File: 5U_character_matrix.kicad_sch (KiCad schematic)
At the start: 14 parts, among them U1 SN74LVC244A, U2 SM411006N/15, U3 SM411006N/15, U4 SN74LVC244A, U5 SM411006N/15, U6 SM411006N/15, U7 SM411006N/15

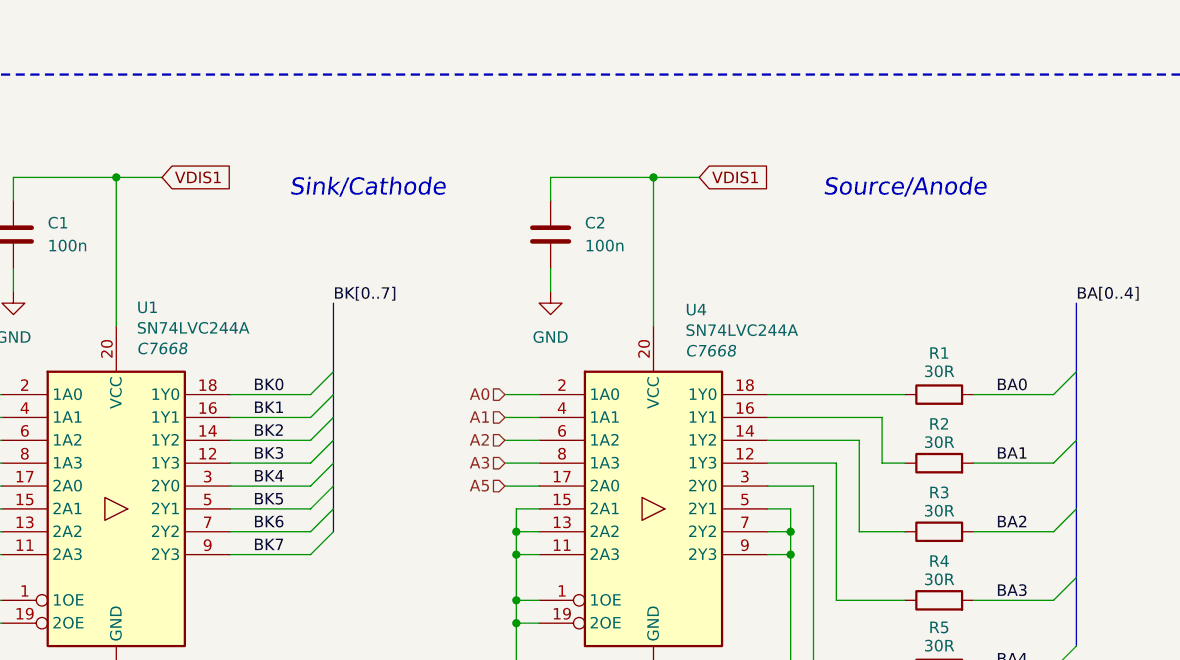
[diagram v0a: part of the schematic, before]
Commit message: power circuit added
- addition of power circuit
- added bypassing circuit
- new formatting of the schematic
- root schematic updated
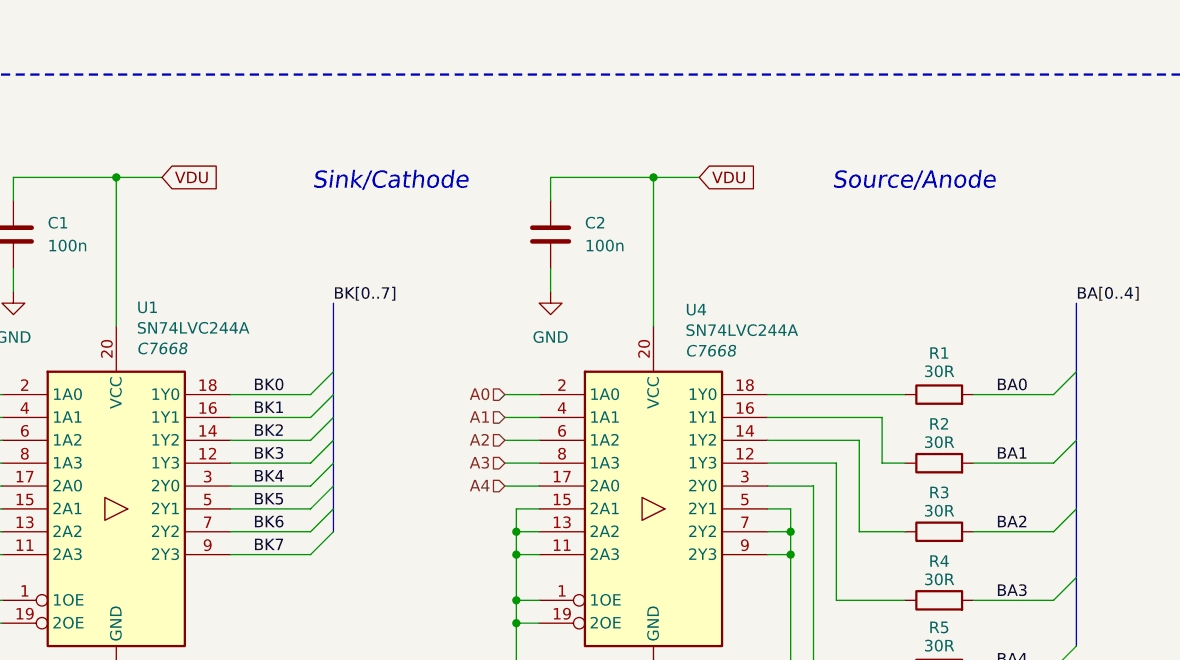
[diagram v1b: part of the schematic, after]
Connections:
- net A5 renamed A4
- net VDIS1 renamed VDU
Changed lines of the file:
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@@
 	(text "Sink/Cathode "
 		(exclude_from_sim no)
-		(at 76.2 114.3 0)
+		(at 78.74 113.538 0)
 		(effects
 			(font
@@
 				(thickness 0.2381)
 				(italic yes)
-				(color 194 0 0 1)
+				(color 132 0 0 1)
 			)
 		)
@@
 	(text "Source/Anode"
 		(exclude_from_sim no)
-		(at 135.89 114.3 0)
+		(at 136.906 113.538 0)
 		(effects
 			(font
@@
 				(thickness 0.2381)
 				(italic yes)
-				(color 194 0 0 1)
+				(color 132 0 0 1)
 			)
 		)
@@
 		)
 	)
-	(global_label "VDIS1"
+	(global_label "VDU"
 		(shape input)
 		(at 113.03 113.03 0)
@@
 		)
 		(property "Intersheetrefs" "${INTERSHEET_REFS}"
-			(at 121.3976 113.03 0)
+			(at 119.7043 113.03 0)
 			(effects
 				(font
@@
 		)
 	)
-	(global_label "VDIS1"
+	(global_label "VDU"
 		(shape input)
 		(at 53.34 113.03 0)
@@
 		)
 		(property "Intersheetrefs" "${INTERSHEET_REFS}"
-			(at 61.7076 113.03 0)
+			(at 60.0143 113.03 0)
 			(effects
 				(font
@@
 		)
 	)
-	(hierarchical_label "A5"
+	(hierarchical_label "A4"
 		(shape input)
 		(at 91.44 147.32 180)
@@
 		(instances
 			(project "Precision Clock"
-				(path "/c9a8ff63-a0d1-4125-9dd1-40fb53daf536/61b252ee-6ab4-4417-a4ad-7fc052d7ca20"
-					(reference "R14")
-					(unit 1)
-				)
 				(path "/c9a8ff63-a0d1-4125-9dd1-40fb53daf536/95a63663-b2f9-448f-a4dd-b71321e8f379"
 					(reference "R4")
@@
 		(instances
 			(project "Precision Clock"
-				(path "/c9a8ff63-a0d1-4125-9dd1-40fb53daf536/61b252ee-6ab4-4417-a4ad-7fc052d7ca20"
-					(reference "U17")
-					(unit 1)
-				)
 				(path "/c9a8ff63-a0d1-4125-9dd1-40fb53daf536/95a63663-b2f9-448f-a4dd-b71321e8f379"
 					(reference "U3")
@@
 		(instances
 			(project "Precision Clock"
-				(path "/c9a8ff63-a0d1-4125-9dd1-40fb53daf536/61b252ee-6ab4-4417-a4ad-7fc052d7ca20"
-					(reference "C5")
-					(unit 1)
-				)
 				(path "/c9a8ff63-a0d1-4125-9dd1-40fb53daf536/95a63663-b2f9-448f-a4dd-b71321e8f379"
 					(reference "C1")
@@
 		(instances
 			(project "Precision Clock"
-				(path "/c9a8ff63-a0d1-4125-9dd1-40fb53daf536/61b252ee-6ab4-4417-a4ad-7fc052d7ca20"
-					(reference "C6")
-					(unit 1)
-				)
 				(path "/c9a8ff63-a0d1-4125-9dd1-40fb53daf536/95a63663-b2f9-448f-a4dd-b71321e8f379"
 					(reference "C2")
@@
 		(instances
 			(project "Precision Clock"
-				(path "/c9a8ff63-a0d1-4125-9dd1-40fb53daf536/61b252ee-6ab4-4417-a4ad-7fc052d7ca20"
-					(reference "U20")
-					(unit 1)
-				)
 				(path "/c9a8ff63-a0d1-4125-9dd1-40fb53daf536/95a63663-b2f9-448f-a4dd-b71321e8f379"
 					(reference "U6")
@@
 		(instances
 			(project "Precision Clock"
-				(path "/c9a8ff63-a0d1-4125-9dd1-40fb53daf536/61b252ee-6ab4-4417-a4ad-7fc052d7ca20"
-					(reference "#PWR09")
-					(unit 1)
-				)
 				(path "/c9a8ff63-a0d1-4125-9dd1-40fb53daf536/95a63663-b2f9-448f-a4dd-b71321e8f379"
 					(reference "#PWR01")
@@
 		(instances
 			(project "Precision Clock"
-				(path "/c9a8ff63-a0d1-4125-9dd1-40fb53daf536/61b252ee-6ab4-4417-a4ad-7fc052d7ca20"
-					(reference "R12")
-					(unit 1)
-				)
 				(path "/c9a8ff63-a0d1-4125-9dd1-40fb53daf536/95a63663-b2f9-448f-a4dd-b71321e8f379"
 					(reference "R2")
@@
 		(instances
 			(project "Precision Clock"
-				(path "/c9a8ff63-a0d1-4125-9dd1-40fb53daf536/61b252ee-6ab4-4417-a4ad-7fc052d7ca20"
-					(reference "U19")
-					(unit 1)
-				)
 				(path "/c9a8ff63-a0d1-4125-9dd1-40fb53daf536/95a63663-b2f9-448f-a4dd-b71321e8f379"
 					(reference "U5")
@@
 		(instances
 			(project "Precision Clock"
-				(path "/c9a8ff63-a0d1-4125-9dd1-40fb53daf536/61b252ee-6ab4-4417-a4ad-7fc052d7ca20"
-					(reference "U15")
-					(unit 1)
-				)
 				(path "/c9a8ff63-a0d1-4125-9dd1-40fb53daf536/95a63663-b2f9-448f-a4dd-b71321e8f379"
 					(reference "U1")
@@
 		(instances
 			(project "Precision Clock"
-				(path "/c9a8ff63-a0d1-4125-9dd1-40fb53daf536/61b252ee-6ab4-4417-a4ad-7fc052d7ca20"
-					(reference "#PWR011")
-					(unit 1)
-				)
 				(path "/c9a8ff63-a0d1-4125-9dd1-40fb53daf536/95a63663-b2f9-448f-a4dd-b71321e8f379"
 					(reference "#PWR03")
@@
 		(instances
 			(project "Precision Clock"
-				(path "/c9a8ff63-a0d1-4125-9dd1-40fb53daf536/61b252ee-6ab4-4417-a4ad-7fc052d7ca20"
-					(reference "U18")
-					(unit 1)
-				)
 				(path "/c9a8ff63-a0d1-4125-9dd1-40fb53daf536/95a63663-b2f9-448f-a4dd-b71321e8f379"
 					(reference "U4")
@@
 		(instances
 			(project "Precision Clock"
-				(path "/c9a8ff63-a0d1-4125-9dd1-40fb53daf536/61b252ee-6ab4-4417-a4ad-7fc052d7ca20"
-					(reference "#PWR010")
-					(unit 1)
-				)
 				(path "/c9a8ff63-a0d1-4125-9dd1-40fb53daf536/95a63663-b2f9-448f-a4dd-b71321e8f379"
 					(reference "#PWR02")
@@
 		(instances
 			(project "Precision Clock"
-				(path "/c9a8ff63-a0d1-4125-9dd1-40fb53daf536/61b252ee-6ab4-4417-a4ad-7fc052d7ca20"
-					(reference "R15")
-					(unit 1)
-				)
 				(path "/c9a8ff63-a0d1-4125-9dd1-40fb53daf536/95a63663-b2f9-448f-a4dd-b71321e8f379"
 					(reference "R5")
@@
 		(instances
 			(project "Precision Clock"
-				(path "/c9a8ff63-a0d1-4125-9dd1-40fb53daf536/61b252ee-6ab4-4417-a4ad-7fc052d7ca20"
-					(reference "#PWR012")
-					(unit 1)
-				)
 				(path "/c9a8ff63-a0d1-4125-9dd1-40fb53daf536/95a63663-b2f9-448f-a4dd-b71321e8f379"
 					(reference "#PWR04")
@@
 		(instances
 			(project "Precision Clock"
-				(path "/c9a8ff63-a0d1-4125-9dd1-40fb53daf536/61b252ee-6ab4-4417-a4ad-7fc052d7ca20"
-					(reference "U21")
-					(unit 1)
-				)
 				(path "/c9a8ff63-a0d1-4125-9dd1-40fb53daf536/95a63663-b2f9-448f-a4dd-b71321e8f379"
 					(reference "U7")
@@
 		(instances
 			(project "Precision Clock"
-				(path "/c9a8ff63-a0d1-4125-9dd1-40fb53daf536/61b252ee-6ab4-4417-a4ad-7fc052d7ca20"
-					(reference "R11")
-					(unit 1)
-				)
 				(path "/c9a8ff63-a0d1-4125-9dd1-40fb53daf536/95a63663-b2f9-448f-a4dd-b71321e8f379"
 					(reference "R1")
@@
 		(instances
 			(project "Precision Clock"
-				(path "/c9a8ff63-a0d1-4125-9dd1-40fb53daf536/61b252ee-6ab4-4417-a4ad-7fc052d7ca20"
-					(reference "R13")
-					(unit 1)
-				)
 				(path "/c9a8ff63-a0d1-4125-9dd1-40fb53daf536/95a63663-b2f9-448f-a4dd-b71321e8f379"
 					(reference "R3")

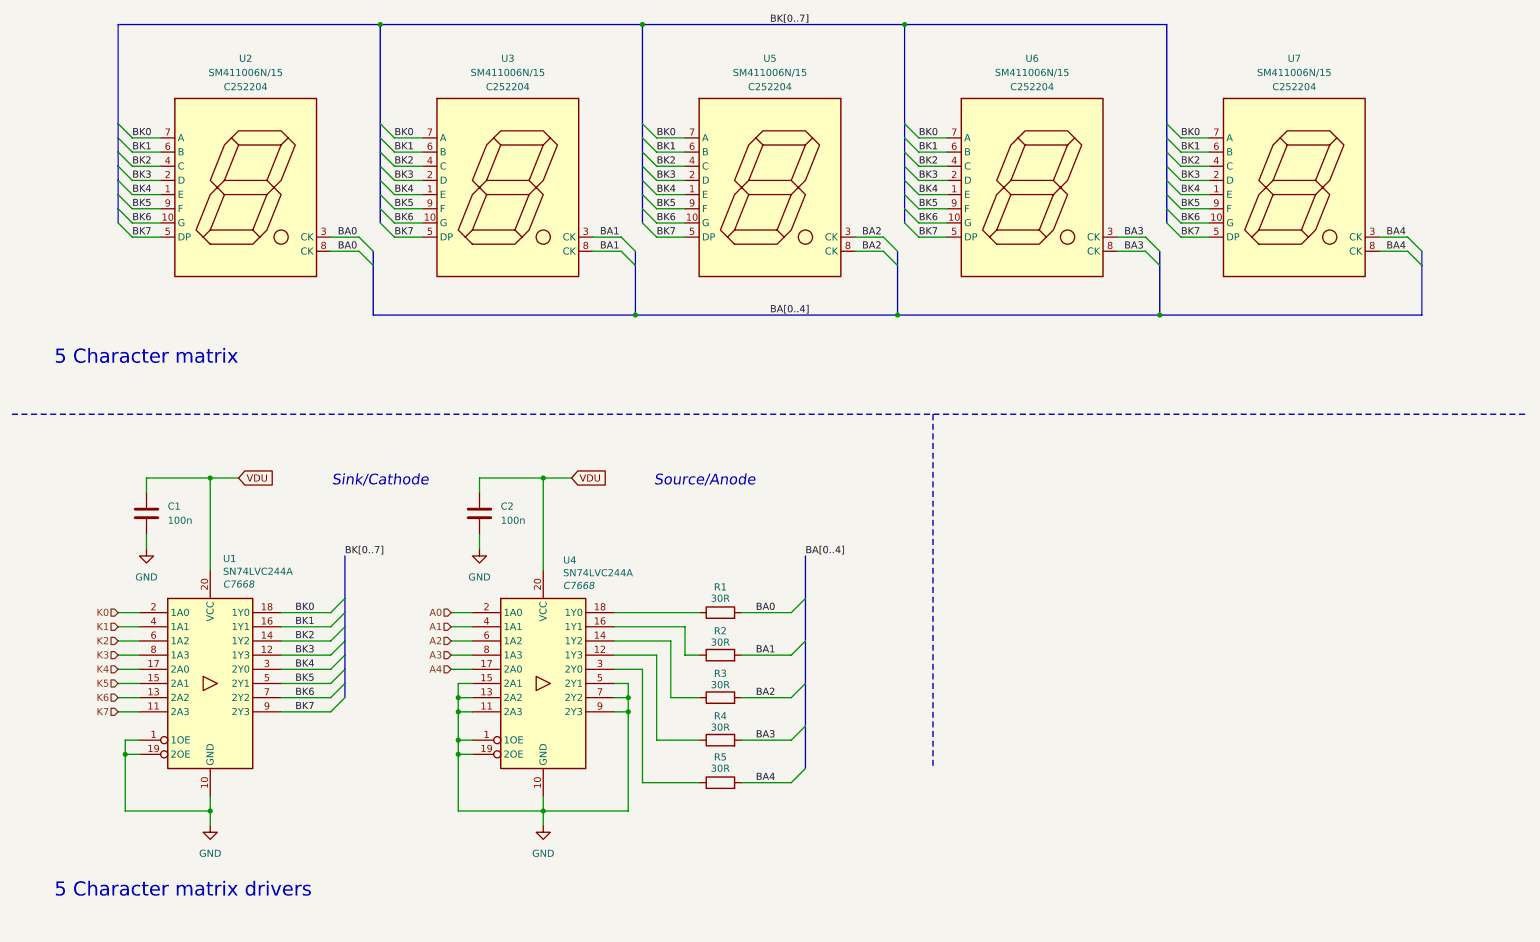
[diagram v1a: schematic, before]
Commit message: addition of bus
- cleaned up the structure of the schematic.
- addition of the colon
- root schematic improvements
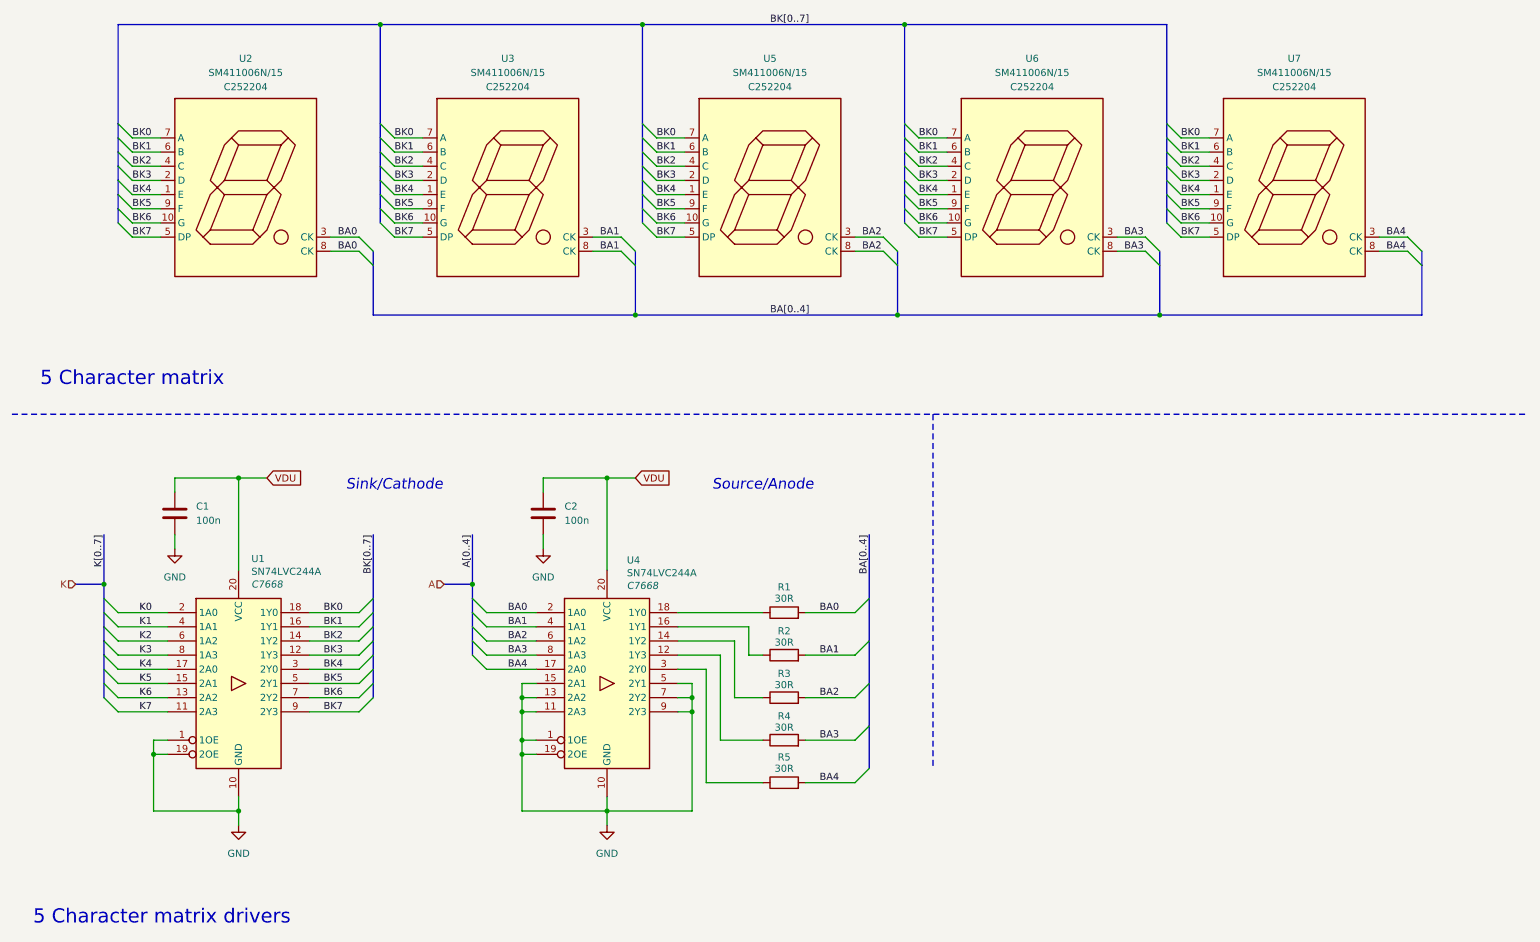
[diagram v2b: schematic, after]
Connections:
- net A0 is gone; now on net BA0: U4.2 (1A0)
- net A1 is gone; now on net BA1: U4.4 (1A1)
- net A2 is gone; now on net BA2: U4.6 (1A2)
- net A3 is gone; now on net BA3: U4.8 (1A3)
- net A4 is gone; now on net BA4: U4.17 (2A0)
